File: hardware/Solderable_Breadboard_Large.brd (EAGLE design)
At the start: 195.6 x 63.5 mm, 161 parts

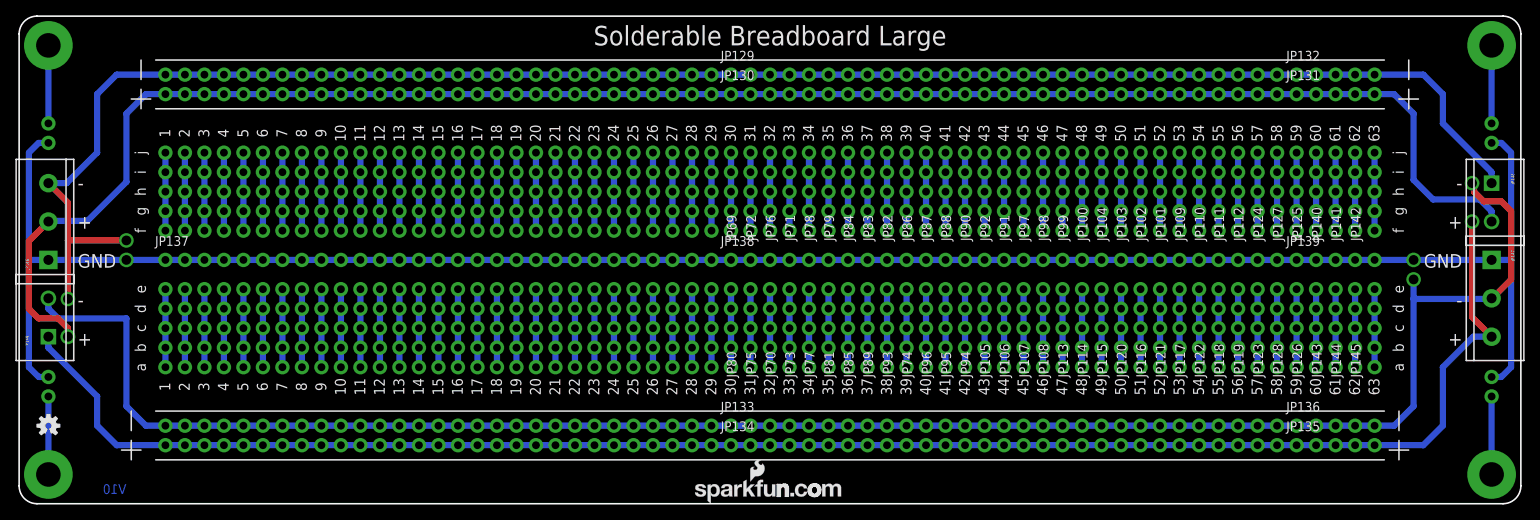
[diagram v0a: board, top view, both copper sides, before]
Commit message: Renamed files to match product name, and updates from reviewing protos.
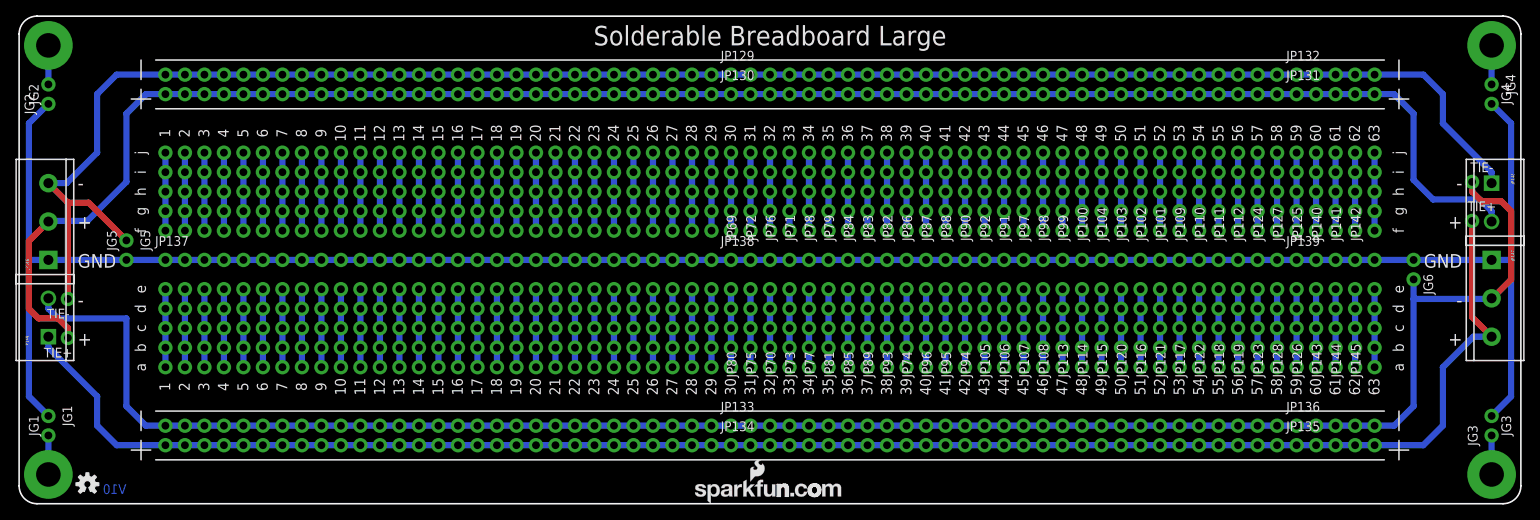
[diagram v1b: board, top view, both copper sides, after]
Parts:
- removed JP150, JP151, JP152, JP153, JP65, JP66, JP67, JP68: M01SMDNS, SparkFun-Connectors:1X01NS
- added JG1, JG2, JG3, JG4, JG5, JG6: M021X02_NO_SILK, SparkFun-Connectors:1X02_NO_SILK
- added TIE+1, TIE+2, TIE-1, TIE-2: M01SMDNS, SparkFun-Connectors:1X01NS
- moved S2 188.0 mm to (3.81, 59.7)
- moved S3 188.0 mm to (191.8, 3.81)
- moved S1 55.9 mm to (3.81, 3.81)
- moved S4 55.9 mm to (191.8, 59.7)
- moved LOGO3 9.16 mm to (8.89, 2.54)
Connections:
- removed net N$65: JP65.1, S2.P1
- removed net N$66: JP66.1, S1.P1
- new net N$1: JG1.2, S1.P1
- new net N$2: JG2.2, S2.P1
- net GND: now also JG1.1, JG2.1, JG3.2, JG4.2, JG5.2, JG6.1; no longer JP150.1, JP151.1, JP152.1, JP153.1
- net N$67: now also JG3.1; no longer JP67.1
- net N$68: now also JG4.1; no longer JP68.1
- net V+BOT: now also TIE+2.1
- net V+TOP: now also TIE+1.1
- net V-BOT: now also JG6.2, TIE-2.1
- net V-TOP: now also JG5.1, TIE-1.1
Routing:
- net GND: track 261.2 -> 278.5 mm, vias 2 -> 0
- net N$66: track 10.2 -> 0.00 mm
- net N$65: track 10.2 -> 0.00 mm
- net N$68: track 10.2 -> 5.08 mm
- net N$67: track 10.2 -> 5.08 mm
- net N$1: track 0.00 -> 5.08 mm
- net N$2: track 0.00 -> 5.08 mm
- net V-TOP: track 231.0 -> 233.0 mm, vias 2 -> 0
- net V-BOT: track 239.5 -> 239.8 mm, vias 2 -> 0
- net V+TOP: track 232.4 -> 232.6 mm, vias 1 -> 0
- net V+BOT: vias 1 -> 0
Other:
- board text added: "JG1"
- board text added: "JG2"
- board text added: "JG3"
- board text added: "JG4"
- board text added: "JG5"
- board text added: "JG6"
- board text added: "TIE+"
- board text added: "TIE-"
